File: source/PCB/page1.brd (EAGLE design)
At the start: 74.9 x 45.7 mm, 25 parts, among them J1 RJ45-MJ88-BX11-RVSL2-3420050P1, J2 CONNECTOR-HEADER-6P-3460650P1, J4 CONNECTOR-HEADER-3P-3460810P1, J5 CONNECTOR-HEADER-2X3P-3460180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, Q1 MOSFET-N-044020001, Q2 MOSFET-N-044020001, Q3 MOSFET-N-044020001, Q4 MOSFET-N-044020001, U1 ATMEGA328P-AU-1030060P1, U2 L298-1420010P1

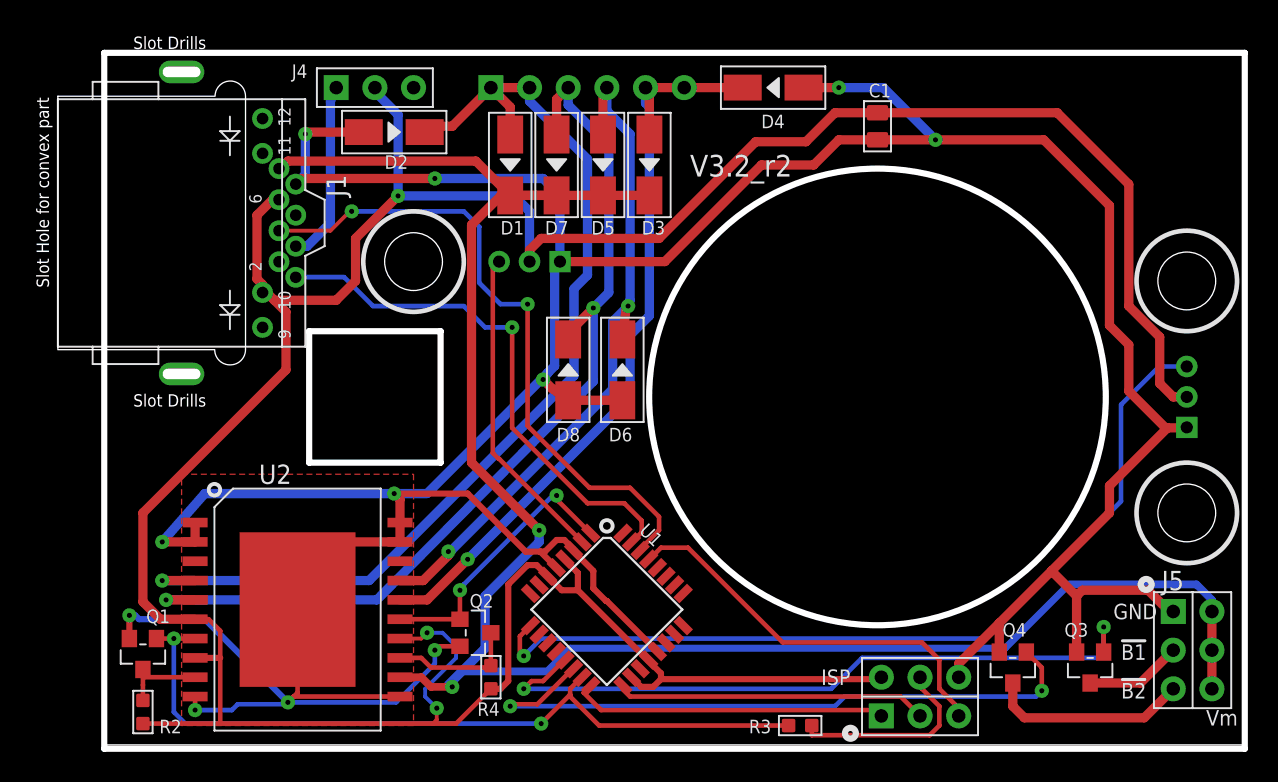
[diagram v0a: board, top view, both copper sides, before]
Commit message: LED board update rev3.  Vs and Vss corrected
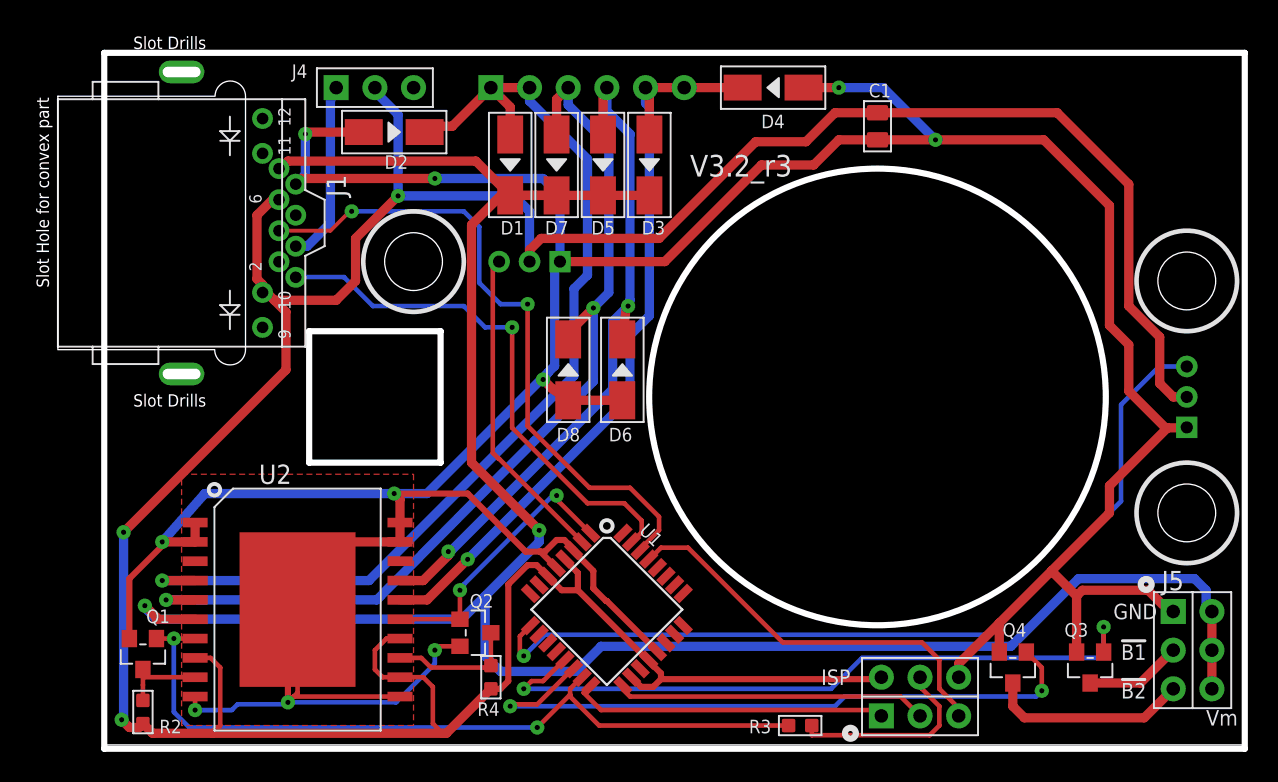
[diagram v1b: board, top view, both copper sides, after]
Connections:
- net +12V: now also U2.6; no longer U2.12
- net +5V: now also U2.12; no longer U2.6
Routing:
- net +12V: track 129.5 -> 147.9 mm
- net +5V: track 215.9 -> 219.5 mm
- net GND: track 269.2 -> 266.5 mm, vias 11 -> 10
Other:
- board text added: "V3.2_r3"
- board text removed: "V3.2_r2"

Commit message: added control over stirrer driver OE
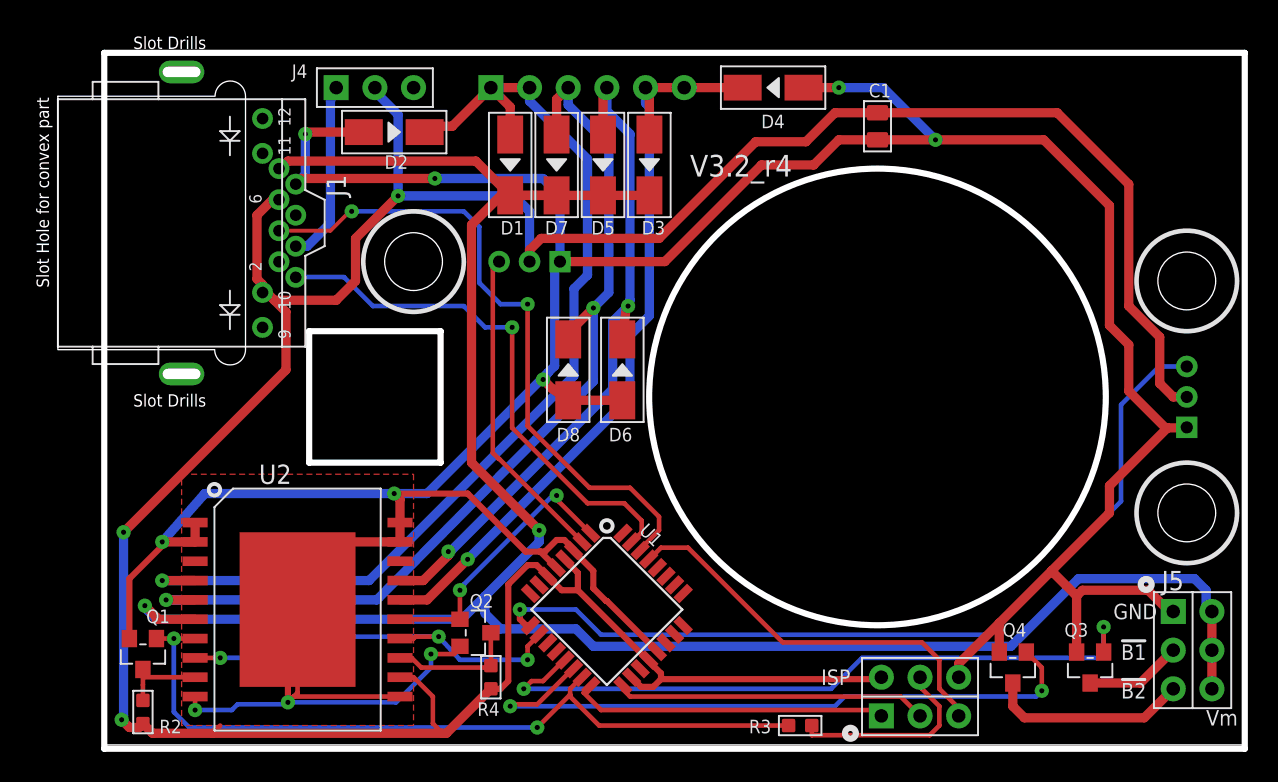
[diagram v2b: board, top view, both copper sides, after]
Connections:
- new net MOTOR_EN: U1.10, U2.14, U2.8
- net +5V: no longer U2.14, U2.8
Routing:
- net MOTOR_EN: track 0.00 -> 27.7 mm, vias 0 -> 3
- net +5V: track 219.5 -> 208.3 mm
- net +12V: track 147.9 -> 144.9 mm
- net LF2: track 57.9 -> 57.0 mm
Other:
- board text added: "V3.2_r4"
- board text removed: "V3.2_r3"
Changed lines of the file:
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@@
 <hole x="71.12" y="30.48" drill="3.7972"/>
 <hole x="71.12" y="15.24" drill="3.7972"/>
-<text x="38.481" y="37.338" size="1.4224" layer="21" font="vector" ratio="15">V3.2_r3</text>
+<text x="38.481" y="37.338" size="1.4224" layer="21" font="vector" ratio="15">V3.2_r4</text>
 <circle x="50.8" y="22.86" radius="15" width="0.4064" layer="46"/>
 <wire x1="22.098" y1="27.178" x2="13.462" y2="27.178" width="0.4064" layer="46"/>
@@
 <wire x1="28.575" y1="14.097" x2="28.575" y2="13.335" width="0.6096" layer="16"/>
 <wire x1="28.575" y1="13.335" x2="25.019" y2="9.779" width="0.6096" layer="16"/>
-<wire x1="25.019" y1="9.779" x2="25.019" y2="5.842" width="0.6096" layer="16"/>
+<wire x1="25.019" y1="9.779" x2="25.019" y2="8.636" width="0.6096" layer="16"/>
 <contactref element="U2" pad="6"/>
 <wire x1="72.771" y1="8.763" x2="72.39" y2="9.144" width="0.6096" layer="16"/>
@@
 <wire x1="71.628" y1="10.922" x2="64.008" y2="10.922" width="0.6096" layer="16"/>
 <wire x1="64.008" y1="10.922" x2="59.563" y2="6.477" width="0.6096" layer="16"/>
-<wire x1="59.563" y1="6.477" x2="32.639" y2="6.477" width="0.6096" layer="16"/>
-<wire x1="32.639" y1="6.477" x2="30.988" y2="4.826" width="0.6096" layer="16"/>
-<wire x1="30.988" y1="4.826" x2="26.035" y2="4.826" width="0.6096" layer="16"/>
-<wire x1="26.035" y1="4.826" x2="25.019" y2="5.842" width="0.6096" layer="16"/>
+<wire x1="59.563" y1="6.477" x2="32.131" y2="6.477" width="0.6096" layer="16"/>
+<wire x1="32.131" y1="6.477" x2="30.988" y2="7.62" width="0.6096" layer="16"/>
+<wire x1="30.988" y1="7.62" x2="26.035" y2="7.62" width="0.6096" layer="16"/>
+<wire x1="26.035" y1="7.62" x2="25.019" y2="8.636" width="0.6096" layer="16"/>
 <wire x1="25.019" y1="9.779" x2="23.495" y2="8.255" width="0.6096" layer="16"/>
 <wire x1="23.495" y1="8.255" x2="3.429" y2="8.255" width="0.6096" layer="16"/>
@@
 <wire x1="33.02" y1="9.455684375" x2="32.962315625" y2="9.455684375" width="0.4064" layer="1"/>
 <wire x1="30.8332" y1="12.773853125" x2="30.914146875" y2="12.773853125" width="0.4064" layer="1"/>
-<wire x1="23.368" y1="6.477" x2="22.098" y2="6.477" width="0.3048" layer="1"/>
-<wire x1="22.098" y1="6.477" x2="21.717" y2="6.223" width="0.3048" layer="1"/>
-<via x="21.717" y="6.223" extent="1-16" drill="0.3302"/>
-<wire x1="21.717" y1="6.223" x2="21.717" y2="5.334" width="0.3048" layer="16"/>
-<wire x1="21.717" y1="5.334" x2="19.177" y2="2.794" width="0.3048" layer="16"/>
+<wire x1="23.368" y1="6.477" x2="22.987" y2="5.969" width="0.3048" layer="1"/>
+<wire x1="22.987" y1="5.969" x2="21.463" y2="5.969" width="0.3048" layer="1"/>
+<via x="21.463" y="5.969" extent="1-16" drill="0.3302"/>
+<wire x1="21.463" y1="5.969" x2="21.463" y2="5.08" width="0.3048" layer="16"/>
+<wire x1="21.463" y1="5.08" x2="19.177" y2="2.794" width="0.3048" layer="16"/>
 <wire x1="19.431" y1="3.175" x2="12.446" y2="3.175" width="0.3048" layer="1"/>
 <wire x1="12.446" y1="3.175" x2="12.065" y2="2.794" width="0.3048" layer="1"/>
@@
 <wire x1="46.101" y1="39.624" x2="48.006" y2="41.529" width="0.6096" layer="1"/>
 <wire x1="48.006" y1="41.529" x2="50.8" y2="41.529" width="0.6096" layer="1"/>
-<contactref element="U2" pad="14"/>
-<contactref element="U2" pad="8"/>
 <contactref element="U2" pad="12"/>
-<wire x1="21.59" y1="3.81" x2="20.955" y2="4.445" width="0.3048" layer="1"/>
-<wire x1="20.955" y1="4.445" x2="19.431" y2="4.445" width="0.3048" layer="1"/>
-<wire x1="19.431" y1="4.445" x2="18.288" y2="4.445" width="0.3048" layer="1"/>
-<wire x1="18.288" y1="4.445" x2="17.78" y2="4.953" width="0.3048" layer="1"/>
-<wire x1="17.78" y1="4.953" x2="17.78" y2="6.223" width="0.3048" layer="1"/>
-<wire x1="17.78" y1="6.223" x2="18.542" y2="6.985" width="0.3048" layer="1"/>
-<wire x1="18.542" y1="6.985" x2="19.431" y2="6.985" width="0.3048" layer="1"/>
+<wire x1="21.59" y1="3.175" x2="20.32" y2="4.445" width="0.3048" layer="1"/>
+<wire x1="20.32" y1="4.445" x2="19.431" y2="4.445" width="0.3048" layer="1"/>
 <wire x1="2.54" y1="1.397" x2="3.175" y2="0.762" width="0.6096" layer="1"/>
 <wire x1="3.175" y1="0.762" x2="7.112" y2="0.762" width="0.6096" layer="1"/>
@@
 <wire x1="22.225" y1="0.762" x2="22.479" y2="0.762" width="0.6096" layer="1"/>
 <wire x1="22.479" y1="0.762" x2="25.4" y2="3.683" width="0.6096" layer="1"/>
-<wire x1="21.59" y1="3.81" x2="21.59" y2="1.397" width="0.3048" layer="1"/>
+<wire x1="21.59" y1="3.175" x2="21.59" y2="1.397" width="0.3048" layer="1"/>
 <wire x1="21.59" y1="1.397" x2="22.225" y2="0.762" width="0.3048" layer="1"/>
-<wire x1="5.969" y1="5.715" x2="6.985" y2="5.715" width="0.3048" layer="1"/>
-<wire x1="6.985" y1="5.715" x2="7.62" y2="5.08" width="0.3048" layer="1"/>
-<wire x1="7.62" y1="5.08" x2="7.62" y2="1.27" width="0.3048" layer="1"/>
 <wire x1="7.62" y1="1.27" x2="7.112" y2="0.762" width="0.3048" layer="1"/>
 <via x="1.27" y="13.97" extent="1-16" drill="0.3302"/>
@@
 <wire x1="66.802" y1="22.352" x2="66.802" y2="16.002" width="0.3048" layer="16"/>
 <wire x1="66.802" y1="16.002" x2="58.039" y2="7.239" width="0.3048" layer="16"/>
-<via x="27.559" y="5.842" extent="1-16" drill="0.3302"/>
-<wire x1="27.305" y1="7.1348" x2="28.004771875" y2="7.834571875" width="0.3048" layer="1"/>
-<wire x1="27.559" y1="5.842" x2="28.956" y2="7.239" width="0.3048" layer="16"/>
-<wire x1="28.956" y1="7.239" x2="58.039" y2="7.239" width="0.3048" layer="16"/>
-<wire x1="27.305" y1="7.1348" x2="27.305" y2="5.969" width="0.3048" layer="1"/>
-<wire x1="27.305" y1="5.969" x2="27.559" y2="6.096" width="0.3048" layer="1"/>
-<wire x1="27.559" y1="6.096" x2="27.559" y2="5.842" width="0.3048" layer="1"/>
+<via x="27.305" y="8.89" extent="1-16" drill="0.3302"/>
+<wire x1="32.639" y1="7.239" x2="58.039" y2="7.239" width="0.3048" layer="16"/>
+<wire x1="28.004771875" y1="7.834571875" x2="27.725428125" y2="7.834571875" width="0.4064" layer="1"/>
+<wire x1="27.725428125" y1="7.834571875" x2="27.305" y2="8.255" width="0.4064" layer="1"/>
+<wire x1="27.305" y1="8.255" x2="27.305" y2="8.89" width="0.4064" layer="1"/>
+<wire x1="32.639" y1="7.239" x2="30.988" y2="8.89" width="0.3048" layer="16"/>
+<wire x1="30.988" y1="8.89" x2="27.305" y2="8.89" width="0.3048" layer="16"/>
 </signal>
 <signal name="OSC2B">
@@
 <contactref element="U2" pad="13"/>
 <wire x1="25.4" y1="5.207" x2="25.4" y2="7.366" width="0.3048" layer="1"/>
-<wire x1="19.431" y1="5.715" x2="20.828" y2="5.715" width="0.3048" layer="1"/>
-<wire x1="20.828" y1="5.715" x2="21.463" y2="5.08" width="0.3048" layer="1"/>
-<wire x1="21.463" y1="5.08" x2="25.019" y2="5.08" width="0.3048" layer="1"/>
+<wire x1="19.431" y1="5.715" x2="20.193" y2="5.715" width="0.3048" layer="1"/>
+<wire x1="20.193" y1="5.715" x2="20.828" y2="5.08" width="0.3048" layer="1"/>
+<wire x1="20.828" y1="5.08" x2="25.019" y2="5.08" width="0.3048" layer="1"/>
 <wire x1="25.019" y1="5.08" x2="25.4" y2="5.207" width="0.3048" layer="1"/>
 </signal>
@@
 <wire x1="68.072" y1="4.064" x2="70.231" y2="6.223" width="0.6096" layer="1"/>
 </signal>
+<signal name="MOTOR_EN" class="1">
+<contactref element="U2" pad="8"/>
+<contactref element="U2" pad="14"/>
+<contactref element="U1" pad="10"/>
+<wire x1="28.570459375" y1="7.268884375" x2="28.570459375" y2="7.234459375" width="0.3048" layer="1"/>
+<wire x1="28.570459375" y1="7.234459375" x2="27.813" y2="6.477" width="0.3048" layer="1"/>
+<wire x1="27.813" y1="6.477" x2="27.813" y2="5.588" width="0.3048" layer="1"/>
+<via x="27.813" y="5.588" extent="1-16" drill="0.3302"/>
+<wire x1="27.813" y1="5.588" x2="23.368" y2="5.588" width="0.3048" layer="16"/>
+<wire x1="23.368" y1="5.588" x2="21.971" y2="7.112" width="0.3048" layer="16"/>
+<via x="21.971" y="7.112" extent="1-16" drill="0.3302"/>
+<wire x1="21.971" y1="7.112" x2="20.447" y2="7.112" width="0.3048" layer="1"/>
+<wire x1="20.447" y1="7.112" x2="20.32" y2="6.985" width="0.3048" layer="1"/>
+<wire x1="20.32" y1="6.985" x2="19.431" y2="6.985" width="0.3048" layer="1"/>
+<wire x1="5.969" y1="5.715" x2="7.62" y2="5.715" width="0.3048" layer="1"/>
+<via x="7.62" y="5.715" extent="1-16" drill="0.3302"/>
+<wire x1="7.62" y1="5.715" x2="11.811" y2="5.715" width="0.3048" layer="16"/>
+<wire x1="11.811" y1="5.715" x2="13.208" y2="7.112" width="0.3048" layer="16"/>
+<wire x1="13.208" y1="7.112" x2="21.971" y2="7.112" width="0.3048" layer="16"/>
+</signal>
 </signals>

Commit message: updated PCB
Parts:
- removed D1, D2, D3, D4, D5, D6, D7, D8: (no value), OPL Eagle Library:DO-214AC
- removed Q1, Q2: MOSFET-N-044020001, OPL Eagle Library:SOT23
- added C2, C3: 100nf, Seeed-OPL-Capacitor:C0805
- added C4: 220nf, Seeed-OPL-Capacitor:C0603
- added CT1: 100uf, Seeed-OPL-Capacitor:ELECTRO-SMD-E-7.8MM
- added R1: 0.2R 1/3W, Seeed-OPL-Resistor:R0805
- added R5: 2.7K, Seeed-OPL-Resistor:R0805
- added R6: 270R, Seeed-OPL-Resistor:R0805
- J1: value RJ45-MJ88-BX11-RVSL2-3420050P1 -> MJ88-BX11-RVSL2; device OPL Eagle Library:RJ45-MJ88-BX11-RVSL2 -> Seeed-OPL-Connector:RJ45-12+2P-16.3X15.4X11.5MM-IN
- R2: value 10k -> 0.2R 1/3W; device OPL Eagle Library:R0603 -> Seeed-OPL-Resistor:R0805
- R4: value 10k -> 22K; device OPL Eagle Library:R0603 -> Seeed-OPL-Resistor:R0805
- U2: value L298-1420010P1 -> A4988SETTR-QFN28; device OPL Eagle Library:POWERSO-20 -> Seeed-OPL-ic:QFN28G_0.5-5X5MM
- moved R2 16.0 mm to (14.5, 12.8), turned to 180 degrees
- moved R4 8.64 mm to (22.9, 12.7)
- moved U2 2.54 mm to (12.7, 6.35)
- moved ISP 0.13 mm to (53.6, 3.05)
- turned J2 to 90 degrees
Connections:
- removed net !A: Q1.3, R2.2, U2.9
- removed net !B: Q2.3, R4.2, U2.13
- removed net M1!A: D7.1, D8.2, J2.3, U2.5
- removed net M1!B: D3.1, D4.2, J2.5, J2.6, U2.16
- removed net MOTOR_EN: U1.10, U2.14, U2.8
- removed net OSC2A: Q1.1, R3.2, U1.15, U2.7
- removed net OSC2B: Q2.1, U1.1, U2.15
- new net M!EN: U1.10, U2.2
- new net M!RST: U1.32, U2.12
- new net M!SLP: U1.12, U2.14
- new net M2A: J2.4, U2.26
- new net M2B: J2.5, J2.6, U2.1
- new net MDIR: U1.11, U2.19
- new net MS1: U1.23, U2.9
- new net MS2: U1.24, U2.10
- new net MS3: U1.25, U2.11
- new net N$10: R4.1, R5.2, U2.17
- new net N$11: J4.3, R6.2
- new net N$2: R2.1, U2.23
- new net N$5: R1.1, U2.27
- new net N$6: C4.2, U2.8
- new net N$7: C2.1, U2.5
- new net N$8: C2.2, U2.4
- new net N$9: C3.1, U2.6
- new net OC2A: R3.2, U1.15
- new net OC2B: U1.1, U2.16
- net +12V: now also C3.2, CT1.+, U2.22, U2.28; no longer D1.2, D3.2, D5.2, D7.2, U2.6
- net +5V: now also R4.2, U2.13, U2.15; no longer R2.1, R4.1, U2.12
- net GND: now also C4.1, CT1.-, R1.2, R2.2, R5.1, U2.18, U2.29, U2.3; no longer D2.1, D4.1, D6.1, D8.1, Q1.2, Q2.2, U2.1, U2.10, U2.11, U2.19, U2.2, U2.20, U2.THERMALS
- net M1A: now also J2.3, U2.24; no longer D1.1, D2.2, J2.1, J2.2, U2.4
- net M1B: now also J2.1, J2.2, U2.21; no longer D5.1, D6.2, J2.4, U2.17
- net N$1: now also R6.1
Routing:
- net M1!A: track 62.9 -> 0.00 mm, vias 2 -> 0
- net M2B: track 0.00 -> 54.6 mm, vias 0 -> 1
- net OSC2A: track 51.5 -> 0.00 mm, vias 2 -> 0
- net M1!B: track 51.2 -> 0.00 mm, vias 1 -> 0
- net GND: track 266.6 -> 215.5 mm, vias 10 -> 21
- net M2A: track 0.00 -> 47.7 mm, vias 0 -> 1
- net MS3: track 0.00 -> 38.9 mm, vias 0 -> 2
- net MS2: track 0.00 -> 37.0 mm, vias 0 -> 2
- net MS1: track 0.00 -> 34.8 mm, vias 0 -> 2
- net M!RST: track 0.00 -> 32.5 mm, vias 0 -> 2
- net MOTOR_EN: track 27.7 -> 0.00 mm, vias 3 -> 0
- net M!EN: track 0.00 -> 25.2 mm, vias 0 -> 2
- net OC2B: track 0.00 -> 23.5 mm, vias 0 -> 2
- net M1A: track 67.4 -> 47.3 mm
- net +12V: track 144.9 -> 164.3 mm, vias 2 -> 1
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- added copper zone on layer 16, net GND
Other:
- board size 74.9 x 45.7 mm -> 74.9 x 45.5 mm
- board text added: "V3.3_r0"
- board text removed: "V3.2_r4"
